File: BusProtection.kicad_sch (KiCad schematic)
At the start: 18 parts, among them Q14 NX3008NBKS, Q15 MBT2222ADW1T1, Q16 NX3008NBKS, Q17 MBT2222ADW1T1

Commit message: Finish v1 schematic
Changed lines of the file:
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@@
 	)
 	(global_label "SCL_Fuel"
-		(shape output)
+		(shape bidirectional)
 		(at 90.297 85.09 0)
 		(fields_autoplaced yes)
@@
 		)
 		(property "Intersheetrefs" "${INTERSHEET_REFS}"
-			(at 101.0946 85.09 0)
+			(at 102.0471 85.09 0)
 			(effects
 				(font
@@
 	)
 	(global_label "SCL1"
-		(shape input)
+		(shape bidirectional)
 		(at 91.44 144.78 180)
 		(fields_autoplaced yes)
@@
 		)
 		(property "Intersheetrefs" "${INTERSHEET_REFS}"
-			(at 84.4713 144.78 0)
+			(at 83.4394 144.78 0)
 			(effects
 				(font
@@
 	)
 	(global_label "SCL_Fuel"
-		(shape output)
+		(shape bidirectional)
 		(at 101.6 144.78 0)
 		(fields_autoplaced yes)
@@
 		)
 		(property "Intersheetrefs" "${INTERSHEET_REFS}"
-			(at 112.3976 144.78 0)
+			(at 113.3501 144.78 0)
 			(effects
 				(font
@@
 	)
 	(global_label "SCL1"
-		(shape input)
+		(shape bidirectional)
 		(at 73.787 76.2 180)
 		(fields_autoplaced yes)
@@
 		)
 		(property "Intersheetrefs" "${INTERSHEET_REFS}"
-			(at 66.8183 76.2 0)
+			(at 65.7864 76.2 0)
 			(effects
 				(font

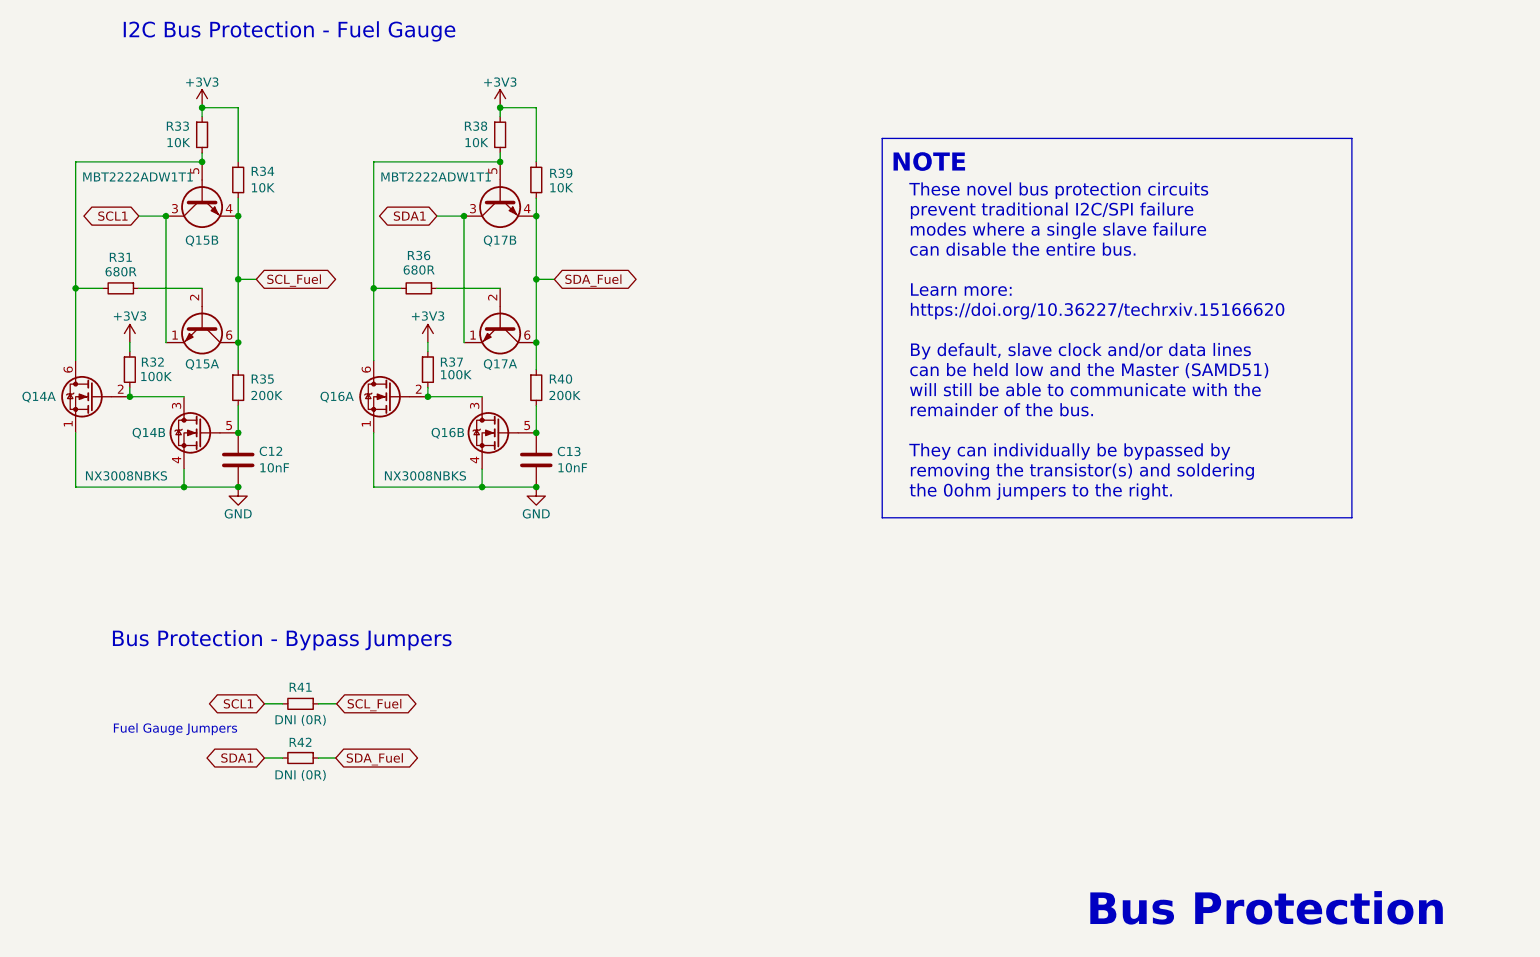
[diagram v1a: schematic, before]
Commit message: Cleanup component designators
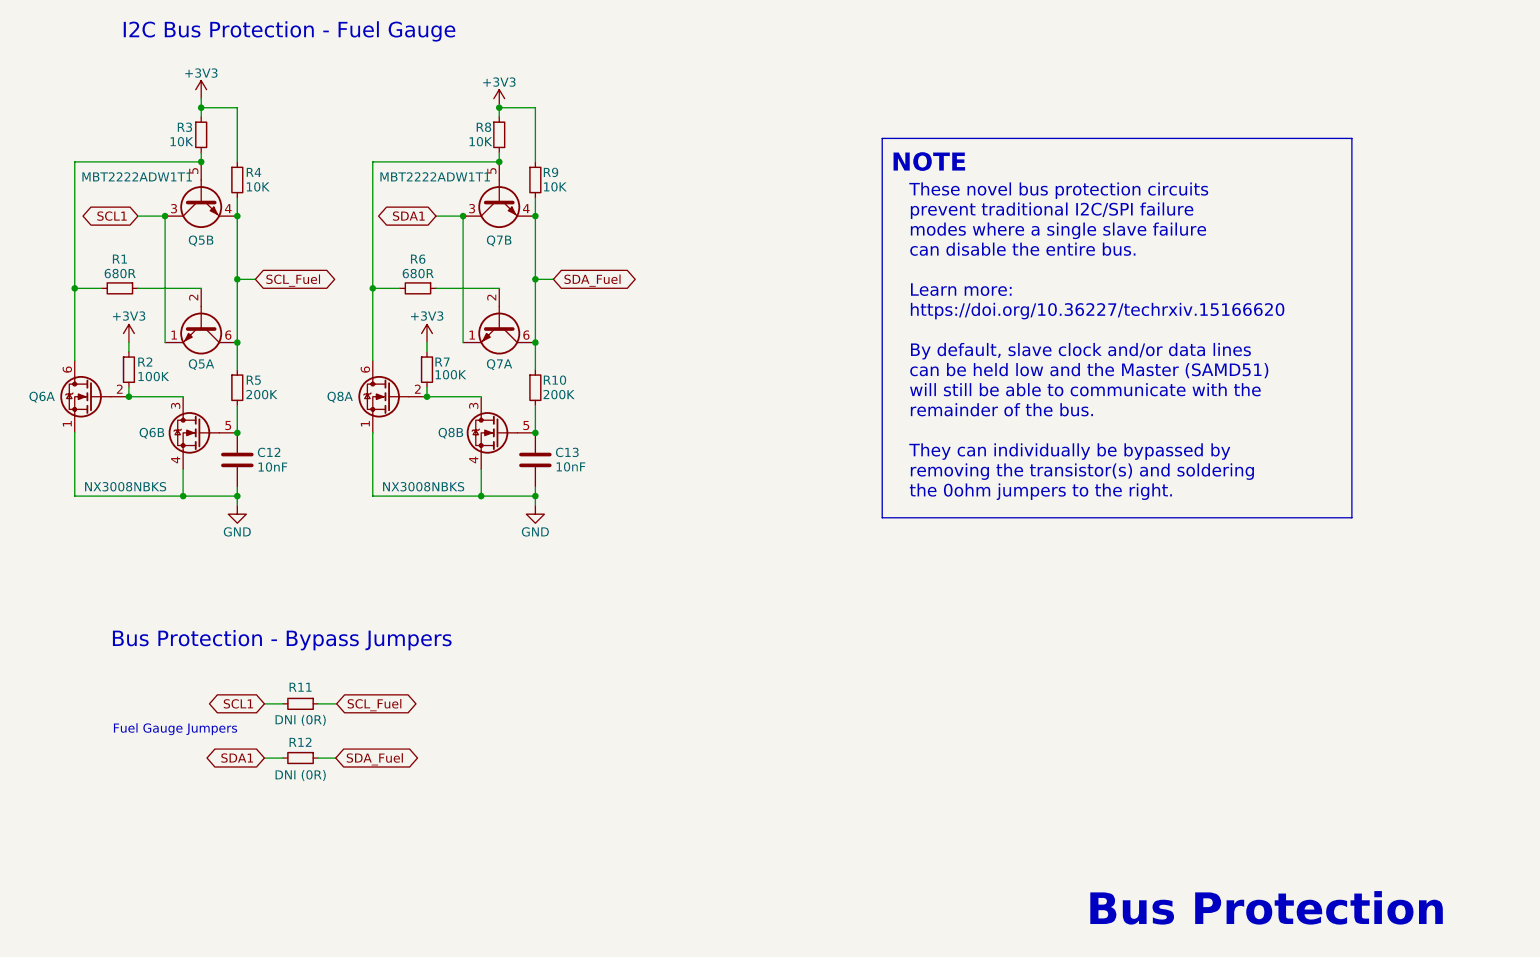
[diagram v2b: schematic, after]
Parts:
- renumbered Q15 to Q5, Q14 to Q6, Q17 to Q7, Q16 to Q8, R31 to R1, R40 to R10, R41 to R11, R42 to R12, R32 to R2, R33 to R3, R34 to R4, R35 to R5, R36 to R6, R37 to R7, R38 to R8, R39 to R9

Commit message: Complete layout
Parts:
- Q6, Q8: symbol mainboard:NX3008NBKS -> BatteryBoard:NX3008NBKS
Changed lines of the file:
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@@
 	(wire
 		(pts
-			(xy 99.06 152.4) (xy 101.473 152.4)
+			(xy 99.06 152.4) (xy 101.6 152.4)
 		)
 		(stroke
@@
 	(global_label "SDA_Fuel"
 		(shape bidirectional)
-		(at 101.473 152.4 0)
+		(at 101.6 152.4 0)
 		(fields_autoplaced yes)
 		(effects
@@
 		)
 		(property "Intersheetrefs" "${INTERSHEET_REFS}"
-			(at 113.2836 152.4 0)
+			(at 113.4106 152.4 0)
 			(effects
 				(font
@@
 			)
 		)
-		(property "Description" ""
+		(property "Description" "Power symbol creates a global label with name \"+3V3\""
 			(at 72.39 93.98 0)
 			(effects
@@
 			)
 		)
-		(property "Description" ""
+		(property "Description" "Power symbol creates a global label with name \"+3V3\""
 			(at 82.55 59.69 0)
 			(effects
@@
 			)
 		)
-		(property "Description" ""
+		(property "Description" "Power symbol creates a global label with name \"+3V3\""
 			(at 124.46 60.96 0)
 			(effects
@@
 	)
 	(symbol
-		(lib_id "mainboard:NX3008NBKS")
+		(lib_id "BatteryBoard:NX3008NBKS")
 		(at 81.28 106.68 0)
 		(mirror y)
@@
 		(dnp no)
 		(property "Reference" "Q6"
-			(at 77.47 106.68 0)
+			(at 77.216 106.68 0)
 			(effects
 				(font
@@
 		)
 		(property "Value" "NX3008NBKS"
-			(at 85.09 111.76 0)
-			(effects
-				(font
-					(size 1.27 1.27)
-				)
-				(justify left)
-				(hide yes)
+			(at 92.964 119.38 0)
+			(effects
+				(font
+					(size 1.27 1.27)
+				)
+				(justify left)
 			)
 		)
@@
 	)
 	(symbol
-		(lib_id "mainboard:NX3008NBKS")
+		(lib_id "BatteryBoard:NX3008NBKS")
 		(at 107.95 101.6 0)
 		(mirror y)
@@
 			)
 		)
-		(property "Description" ""
+		(property "Description" "Power symbol creates a global label with name \"+3V3\""
 			(at 114.3 93.98 0)
 			(effects
@@
 			)
 		)
-		(property "Description" ""
+		(property "Description" "Power symbol creates a global label with name \"GND\" , ground"
 			(at 129.54 116.84 0)
 			(effects
@@
 			)
 		)
-		(property "Description" ""
+		(property "Description" "Power symbol creates a global label with name \"GND\" , ground"
 			(at 87.63 116.84 0)
 			(effects
@@
 	)
 	(symbol
-		(lib_id "mainboard:NX3008NBKS")
+		(lib_id "BatteryBoard:NX3008NBKS")
 		(at 66.04 101.6 0)
 		(mirror y)
@@
 	)
 	(symbol
-		(lib_id "mainboard:NX3008NBKS")
+		(lib_id "BatteryBoard:NX3008NBKS")
 		(at 123.19 106.68 0)
 		(mirror y)

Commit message: Relabeled I2C nets for accuracy
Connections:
- net SCL1 renamed SCL
- net SDA1 renamed SDA
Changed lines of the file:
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@@
 		)
 	)
-	(global_label "SDA1"
+	(global_label "SDA"
 		(shape bidirectional)
 		(at 115.57 76.2 180)
@@
 		)
 		(property "Intersheetrefs" "${INTERSHEET_REFS}"
-			(at 107.5883 76.2 0)
+			(at 108.7184 76.2 0)
 			(effects
 				(font
@@
 		)
 	)
-	(global_label "SCL1"
+	(global_label "SCL"
 		(shape bidirectional)
 		(at 91.44 144.78 180)
@@
 		)
 		(property "Intersheetrefs" "${INTERSHEET_REFS}"
-			(at 83.4394 144.78 0)
+			(at 84.6489 144.78 0)
 			(effects
 				(font
@@
 		)
 	)
-	(global_label "SCL1"
+	(global_label "SCL"
 		(shape bidirectional)
 		(at 73.66 76.2 180)
@@
 		)
 		(property "Intersheetrefs" "${INTERSHEET_REFS}"
-			(at 65.6594 76.2 0)
+			(at 66.8689 76.2 0)
 			(effects
 				(font
@@
 		)
 	)
-	(global_label "SDA1"
+	(global_label "SDA"
 		(shape bidirectional)
 		(at 91.44 152.4 180)
@@
 		)
 		(property "Intersheetrefs" "${INTERSHEET_REFS}"
-			(at 83.4583 152.4 0)
+			(at 84.5884 152.4 0)
 			(effects
 				(font
@@
 				)
 				(justify left)
-			)
-		)
+				(hide yes)
+			)
+		)
